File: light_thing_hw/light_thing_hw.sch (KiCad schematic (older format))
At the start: 60 parts, among them J1 CONNECTORS, J2 Li-Ion Battery, J3 ADDR_LED_PANEL_1_CONNECTORS, J4 ADDR_LED_PANEL_2_CONNECTORS, J5 MIC_CONN, Q1 MMBF170, Q2 BSS83P, SW1 ST_USER_BUTTON1, SW2 ST_RESET_BUTTON, U1 BC832-V1, U2 LSM6DS3, U3 MCP73833T-FCI_UN, U4 LMR62421XMF, U5 LP38511MRX-ADJ_NOPB, U6 STM32L476RGTx

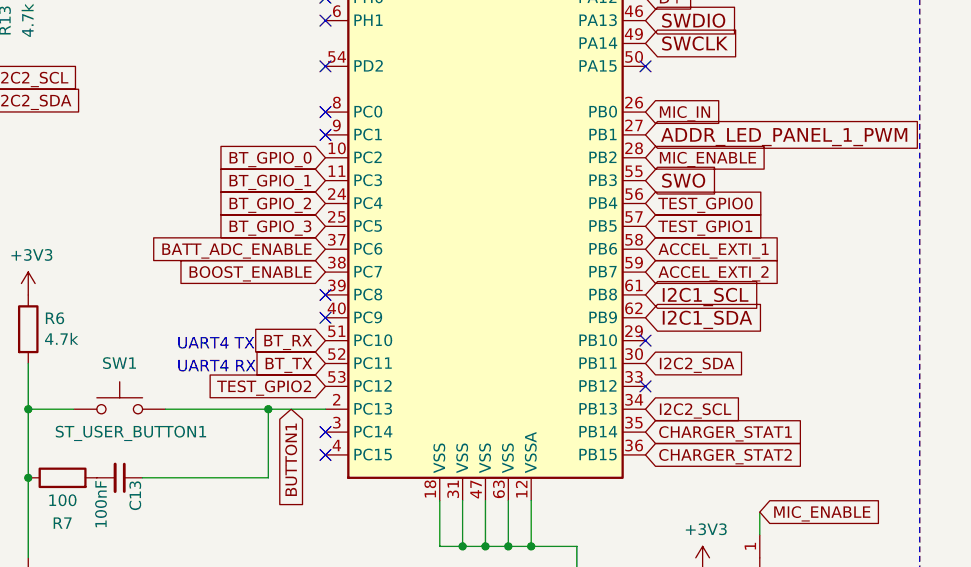
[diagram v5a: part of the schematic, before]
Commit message: about to change diode footprint to something thats available in digikey
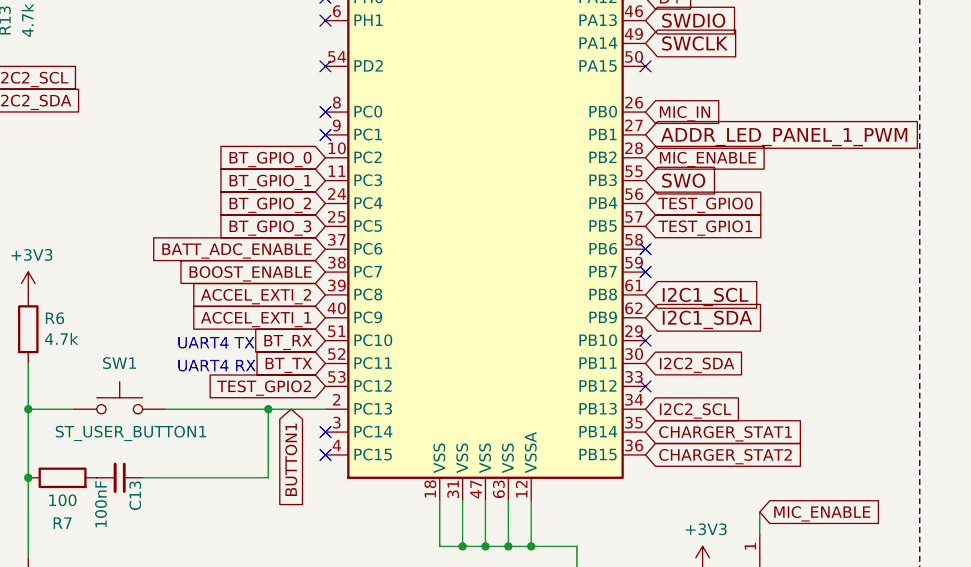
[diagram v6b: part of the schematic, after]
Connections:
- net ACCEL_EXTI_1: now also U6.40 (PC9); no longer U6.58 (PB6)
- net ACCEL_EXTI_2: now also U6.39 (PC8); no longer U6.59 (PB7)
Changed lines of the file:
@@
 Text GLabel 10000 3000 2    50   Input ~ 0
 MIC_ENABLE
-Text GLabel 10000 3400 2    50   Input ~ 0
+Text GLabel 8600 3700 0    50   Input ~ 0
 ACCEL_EXTI_1
-Text GLabel 10000 3500 2    50   Input ~ 0
+Text GLabel 8600 3600 0    50   Input ~ 0
 ACCEL_EXTI_2
 Text GLabel 8600 3400 0    50   Input ~ 0
@@
 NoConn ~ 8600 4300
 NoConn ~ 8600 4200
-NoConn ~ 8600 3700
-NoConn ~ 8600 3600
 NoConn ~ 8600 2900
 NoConn ~ 8600 2800
@@
 Text GLabel 8600 4000 0    50   Input ~ 0
 TEST_GPIO2
+NoConn ~ 10000 3400
+NoConn ~ 10000 3500
 $EndSCHEMATC

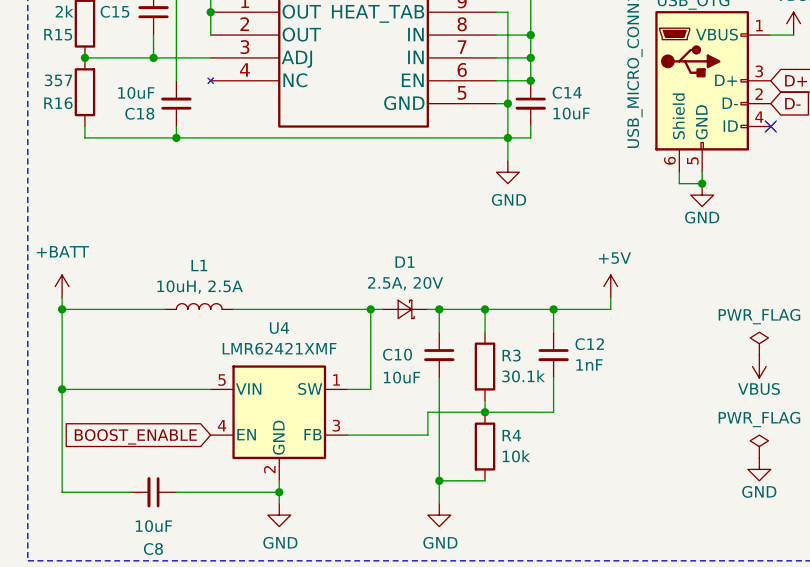
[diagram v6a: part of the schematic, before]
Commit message: picked new reset button and diode footprint
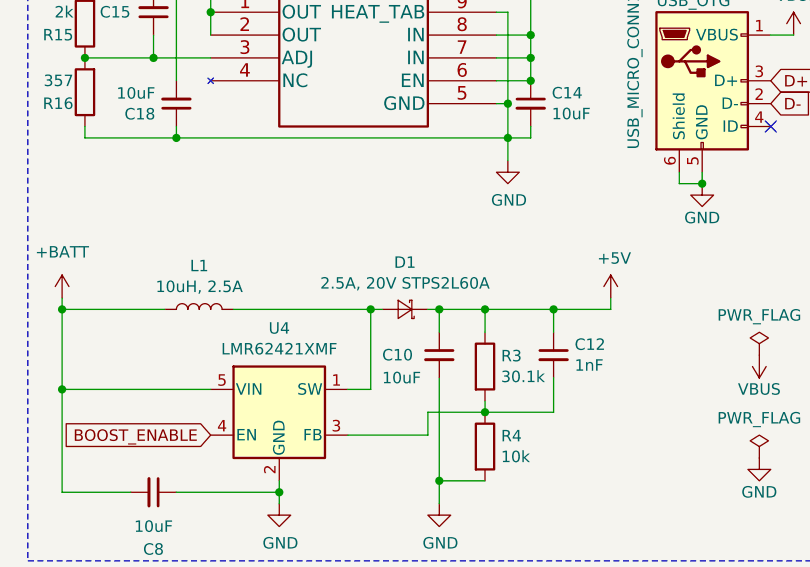
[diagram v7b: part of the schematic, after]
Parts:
- D1: value 2.5A, 20V -> 2.5A, 20V STPS2L60A; footprint Diode_SMD:D_SOD-323_HandSoldering -> Diode_SMD:D_SMA
- SW2: footprint Button_Switch_SMD:SW_SPST_EVPBF -> Button_Switch_SMD:SW_SPST_PTS645
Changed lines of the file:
@@
 F 0 "SW2" H 7900 1400 50  0000 C CNN
 F 1 "ST_RESET_BUTTON" H 8150 1300 50  0000 C CNN
-F 2 "Button_Switch_SMD:SW_SPST_EVPBF" H 7900 1300 50  0001 C CNN
+F 2 "Button_Switch_SMD:SW_SPST_PTS645" H 7900 1300 50  0001 C CNN
 F 3 "" H 7900 1300 50  0001 C CNN
 	1    7900 1100
@@
 P 2150 4100
 F 0 "D1" H 2150 3895 50  0000 C CNN
-F 1 "2.5A, 20V" H 2150 3986 50  0000 C CNN
-F 2 "Diode_SMD:D_SOD-323_HandSoldering" V 2150 4100 50  0001 C CNN
+F 1 "2.5A, 20V  STPS2L60A" H 2150 3986 50  0000 C CNN
+F 2 "Diode_SMD:D_SMA" V 2150 4100 50  0001 C CNN
 F 3 "~" V 2150 4100 50  0001 C CNN
 	1    2150 4100

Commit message: board bringup time
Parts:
- C1, C11, C13, C16, C17, C2, C3, C4, C9: JLC_LIBRARY (none) -> C14663
- R1, R14, R17, R2: JLC_LIBRARY (none) -> C21190
- R10, R11, R12, R13, R6: JLC_LIBRARY (none) -> C23162
- R15: JLC_LIBRARY (none) -> C22975
- R16: JLC_LIBRARY (none) -> C23028
- R18: JLC_LIBRARY (none) -> C17617
- R3: JLC_LIBRARY (none) -> C51221
- R4, R5: JLC_LIBRARY (none) -> C25804
- R7: JLC_LIBRARY (none) -> C22775
- R8, R9: JLC_LIBRARY (none) -> C23193
- U6: JLC_LIBRARY (none) -> C74797
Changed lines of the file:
@@
 EESchema Schematic File Version 4
-LIBS:light_thing_hw-cache
-EELAYER 26 0
+EELAYER 30 0
 EELAYER END
 $Descr A4 11693 8268
@@
 F 2 "Capacitor_SMD:C_0603_1608Metric_Pad1.05x0.95mm_HandSolder" H 7900 1350 50  0001 C CNN
 F 3 "" H 7900 1350 50  0001 C CNN
+F 4 "C14663" H 7900 1350 50  0001 C CNN "JLC_LIBRARY"
 	1    7900 1350
 	0    1    1    0
@@
 F 2 "Resistor_SMD:R_0603_1608Metric_Pad1.05x0.95mm_HandSolder" V 8530 1650 50  0001 C CNN
 F 3 "" H 8600 1650 50  0001 C CNN
+F 4 "C25804" H 8600 1650 50  0001 C CNN "JLC_LIBRARY"
 	1    8600 1650
 	1    0    0    -1
@@
 F 2 "Resistor_SMD:R_0603_1608Metric_Pad1.05x0.95mm_HandSolder" V 2430 4350 50  0001 C CNN
 F 3 "~" H 2500 4350 50  0001 C CNN
+F 4 "C51221" H 2500 4350 50  0001 C CNN "JLC_LIBRARY"
 	1    2500 4350
 	1    0    0    -1
@@
 F 2 "Resistor_SMD:R_0603_1608Metric_Pad1.05x0.95mm_HandSolder" V 2430 4700 50  0001 C CNN
 F 3 "~" H 2500 4700 50  0001 C CNN
+F 4 "C25804" H 2500 4700 50  0001 C CNN "JLC_LIBRARY"
 	1    2500 4700
 	1    0    0    -1
@@
 F 2 "Capacitor_SMD:C_0603_1608Metric_Pad1.05x0.95mm_HandSolder" H 5500 5900 50  0001 C CNN
 F 3 "~" H 5500 5900 50  0001 C CNN
+F 4 "C14663" H 5500 5900 50  0001 C CNN "JLC_LIBRARY"
 	1    5500 5900
 	1    0    0    -1
@@
 F 2 "Capacitor_SMD:C_0603_1608Metric_Pad1.05x0.95mm_HandSolder" H 7700 4400 50  0001 C CNN
 F 3 "" H 7700 4400 50  0001 C CNN
+F 4 "C14663" H 7700 4400 50  0001 C CNN "JLC_LIBRARY"
 	1    7700 4400
 	0    1    1    0
@@
 F 2 "Resistor_SMD:R_0603_1608Metric_Pad1.05x0.95mm_HandSolder" V 7380 4400 50  0001 C CNN
 F 3 "~" H 7450 4400 50  0001 C CNN
+F 4 "C22775" H 7450 4400 50  0001 C CNN "JLC_LIBRARY"
 	1    7450 4400
 	0    -1   -1   0
@@
 F 2 "Resistor_SMD:R_0603_1608Metric_Pad1.05x0.95mm_HandSolder" V 7230 3750 50  0001 C CNN
 F 3 "~" H 7300 3750 50  0001 C CNN
+F 4 "C23162" H 7300 3750 50  0001 C CNN "JLC_LIBRARY"
 	1    7300 3750
 	1    0    0    -1
@@
 F 2 "Resistor_SMD:R_0603_1608Metric_Pad1.05x0.95mm_HandSolder" V 6530 1050 50  0001 C CNN
 F 3 "~" H 6600 1050 50  0001 C CNN
+F 4 "C23193" H 6600 1050 50  0001 C CNN "JLC_LIBRARY"
 	1    6600 1050
 	0    1    1    0
@@
 F 2 "Resistor_SMD:R_0603_1608Metric_Pad1.05x0.95mm_HandSolder" V 6530 1650 50  0001 C CNN
 F 3 "~" H 6600 1650 50  0001 C CNN
+F 4 "C23193" H 6600 1650 50  0001 C CNN "JLC_LIBRARY"
 	1    6600 1650
 	0    1    1    0
@@
 F 2 "Resistor_SMD:R_0603_1608Metric_Pad1.05x0.95mm_HandSolder" V 6980 2450 50  0001 C CNN
 F 3 "~" H 7050 2450 50  0001 C CNN
+F 4 "C23162" H 7050 2450 50  0001 C CNN "JLC_LIBRARY"
 	1    7050 2450
 	1    0    0    -1
@@
 F 2 "Resistor_SMD:R_0603_1608Metric_Pad1.05x0.95mm_HandSolder" V 6880 2450 50  0001 C CNN
 F 3 "~" H 6950 2450 50  0001 C CNN
+F 4 "C23162" H 6950 2450 50  0001 C CNN "JLC_LIBRARY"
 	1    6950 2450
 	1    0    0    -1
@@
 F 2 "Resistor_SMD:R_0603_1608Metric_Pad1.05x0.95mm_HandSolder" V 6230 2450 50  0001 C CNN
 F 3 "~" H 6300 2450 50  0001 C CNN
+F 4 "C23162" H 6300 2450 50  0001 C CNN "JLC_LIBRARY"
 	1    6300 2450
 	1    0    0    -1
@@
 F 2 "Resistor_SMD:R_0603_1608Metric_Pad1.05x0.95mm_HandSolder" V 6130 2450 50  0001 C CNN
 F 3 "~" H 6200 2450 50  0001 C CNN
+F 4 "C23162" H 6200 2450 50  0001 C CNN "JLC_LIBRARY"
 	1    6200 2450
 	1    0    0    -1
@@
 F 2 "Resistor_SMD:R_0603_1608Metric_Pad1.05x0.95mm_HandSolder" V 6780 3350 50  0001 C CNN
 F 3 "~" H 6850 3350 50  0001 C CNN
+F 4 "C21190" H 6850 3350 50  0001 C CNN "JLC_LIBRARY"
 	1    6850 3350
 	-1   0    0    1
@@
 F 2 "Resistor_SMD:R_0603_1608Metric_Pad1.05x0.95mm_HandSolder" V 6780 3750 50  0001 C CNN
 F 3 "~" H 6850 3750 50  0001 C CNN
+F 4 "C21190" H 6850 3750 50  0001 C CNN "JLC_LIBRARY"
 	1    6850 3750
 	1    0    0    -1
@@
 F 2 "Capacitor_SMD:C_0603_1608Metric_Pad1.05x0.95mm_HandSolder" H 4200 1100 50  0001 C CNN
 F 3 "" H 4200 1100 50  0001 C CNN
+F 4 "C14663" H 4200 1100 50  0001 C CNN "JLC_LIBRARY"
 	1    4200 1100
 	1    0    0    -1
@@
 F 2 "Capacitor_SMD:C_0603_1608Metric_Pad1.05x0.95mm_HandSolder" H 4450 1100 50  0001 C CNN
 F 3 "" H 4450 1100 50  0001 C CNN
+F 4 "C14663" H 4450 1100 50  0001 C CNN "JLC_LIBRARY"
 	1    4450 1100
 	1    0    0    -1
@@
 F 2 "Capacitor_SMD:C_0603_1608Metric_Pad1.05x0.95mm_HandSolder" H 4700 1100 50  0001 C CNN
 F 3 "" H 4700 1100 50  0001 C CNN
+F 4 "C14663" H 4700 1100 50  0001 C CNN "JLC_LIBRARY"
 	1    4700 1100
 	1    0    0    -1
@@
 F 2 "Capacitor_SMD:C_0603_1608Metric_Pad1.05x0.95mm_HandSolder" H 4950 1100 50  0001 C CNN
 F 3 "" H 4950 1100 50  0001 C CNN
+F 4 "C14663" H 4950 1100 50  0001 C CNN "JLC_LIBRARY"
 	1    4950 1100
 	1    0    0    -1
@@
 F 2 "Capacitor_SMD:C_0603_1608Metric_Pad1.05x0.95mm_HandSolder" H 5200 1100 50  0001 C CNN
 F 3 "" H 5200 1100 50  0001 C CNN
+F 4 "C14663" H 5200 1100 50  0001 C CNN "JLC_LIBRARY"
 	1    5200 1100
 	1    0    0    -1
@@
 F 2 "Capacitor_SMD:C_0603_1608Metric_Pad1.05x0.95mm_HandSolder" H 5450 1100 50  0001 C CNN
 F 3 "" H 5450 1100 50  0001 C CNN
+F 4 "C14663" H 5450 1100 50  0001 C CNN "JLC_LIBRARY"
 	1    5450 1100
 	1    0    0    -1
@@
 F 2 "Resistor_SMD:R_0603_1608Metric_Pad1.05x0.95mm_HandSolder" V 680 2850 50  0001 C CNN
 F 3 "~" H 750 2850 50  0001 C CNN
+F 4 " C22975" H 750 2850 50  0001 C CNN "JLC_LIBRARY"
 	1    750  2850
 	-1   0    0    1
@@
 F 2 "Resistor_SMD:R_0603_1608Metric_Pad1.05x0.95mm_HandSolder" V 680 3150 50  0001 C CNN
 F 3 "~" H 750 3150 50  0001 C CNN
+F 4 "C23028" H 750 3150 50  0001 C CNN "JLC_LIBRARY"
 	1    750  3150
 	-1   0    0    1
@@
 F 2 "Resistor_SMD:R_0603_1608Metric_Pad1.05x0.95mm_HandSolder" V 1280 1400 50  0001 C CNN
 F 3 "~" H 1350 1400 50  0001 C CNN
+F 4 "C21190" H 1350 1400 50  0001 C CNN "JLC_LIBRARY"
 	1    1350 1400
 	0    -1   -1   0
@@
 F 2 "Resistor_SMD:R_0603_1608Metric_Pad1.05x0.95mm_HandSolder" V 1580 1050 50  0001 C CNN
 F 3 "~" H 1650 1050 50  0001 C CNN
+F 4 "C21190" H 1650 1050 50  0001 C CNN "JLC_LIBRARY"
 	1    1650 1050
 	1    0    0    -1
@@
 F 2 "Resistor_SMD:R_0603_1608Metric_Pad1.05x0.95mm_HandSolder" V 5430 3750 50  0001 C CNN
 F 3 "~" H 5500 3750 50  0001 C CNN
+F 4 "C17617" H 5500 3750 50  0001 C CNN "JLC_LIBRARY"
 	1    5500 3750
 	0    1    1    0
@@
 F 2 "Package_QFP:LQFP-64_10x10mm_P0.5mm" H 8700 1000 50  0001 R CNN
 F 3 "http://www.st.com/st-web-ui/static/active/en/resource/technical/document/datasheet/DM00108832.pdf" H 9300 2700 50  0001 C CNN
+F 4 "C74797" H 9300 2700 50  0001 C CNN "JLC_LIBRARY"
 	1    9300 2700
 	1    0    0    -1
